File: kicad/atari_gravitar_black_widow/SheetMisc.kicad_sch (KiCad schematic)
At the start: 24 parts, among them J17 cat_box_con, J19 J19, J20 J20

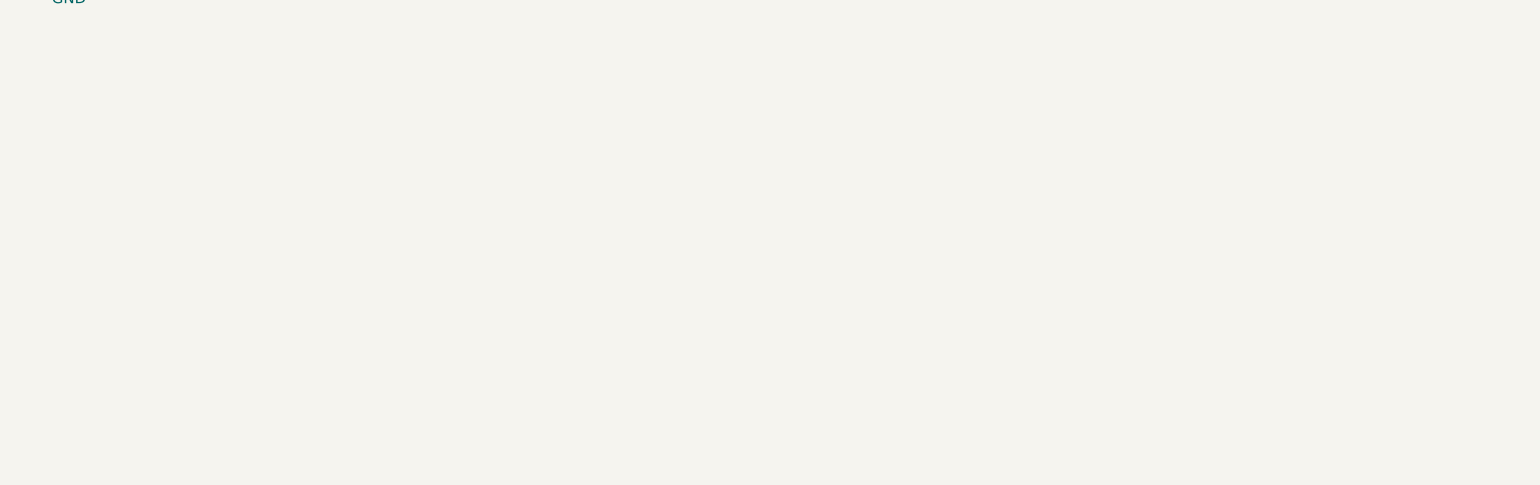
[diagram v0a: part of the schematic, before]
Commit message: NOT LOADED PARTS ADDED
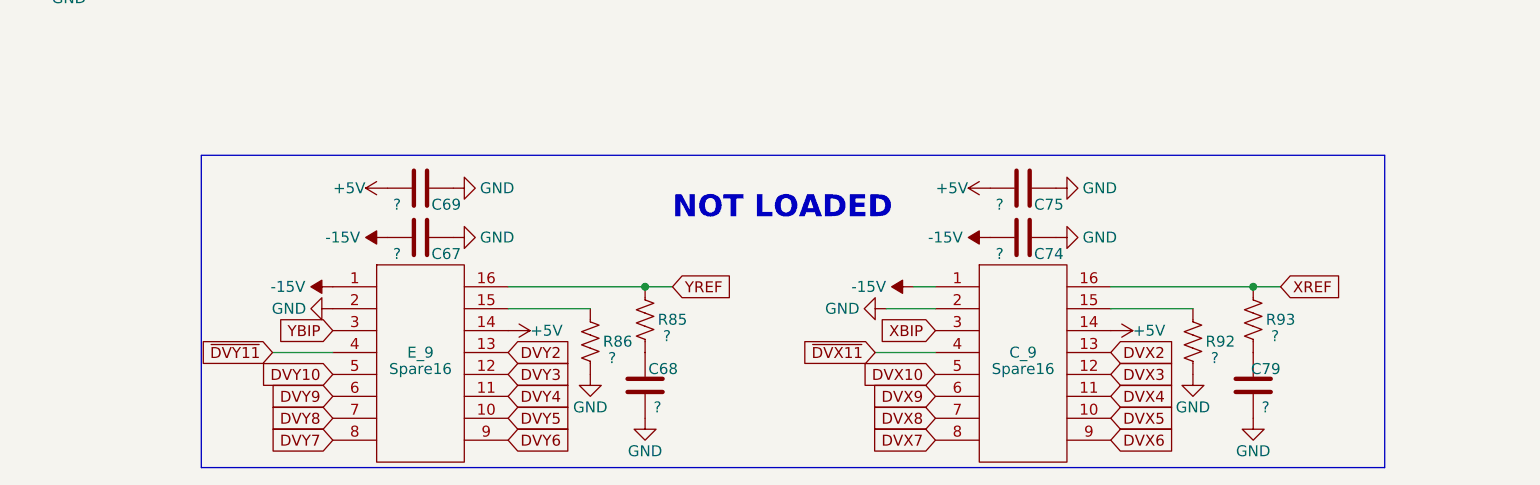
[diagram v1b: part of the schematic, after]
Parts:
- added C67, C69, C74, C75: ?, Star_Wars_Vector_PCB:GenericComp, symbol Device:C
- added C68, C79: ?, Star_Wars_Vector_PCB:CapBrown, symbol Device:C
- added C_9, E_9: Spare16, Star_Wars_Vector_PCB:DIP16, symbol quantum_arcade_pcb:Spare16
- added R85, R86, R92, R93: ?, Star_Wars_Vector_PCB:GenericComp, symbol Device:R_US
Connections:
- net +5V: now also C69.2, C75.2, C_9.14, E_9.14
- net GND: now also C67.1, C68.1, C69.1, C74.1, C75.1, C79.1, C_9.2, E_9.2, R86.1, R92.1
- new net: E_9.15, R86.2
- new net: C68.2, R85.1
- new net: C_9.15, R92.2
- new net: C79.2, R93.1
- new net -15V: C67.2, C74.2, C_9.1, E_9.1
- new net DVX10: C_9.5
- new net DVX2: C_9.13
- new net DVX3: C_9.12
- new net DVX4: C_9.11
- new net DVX5: C_9.10
- new net DVX6: C_9.9
- new net DVX7: C_9.8
- new net DVX8: C_9.7
- new net DVX9: C_9.6
- new net DVY10: E_9.5
- new net DVY2: E_9.13
- new net DVY3: E_9.12
- new net DVY4: E_9.11
- new net DVY5: E_9.10
- new net DVY6: E_9.9
- new net DVY7: E_9.8
- new net DVY8: E_9.7
- new net DVY9: E_9.6
- new net XBIP: C_9.3
- new net XREF: C_9.16, R93.2
- new net YBIP: E_9.3
- new net YREF: E_9.16, R85.2
- new net ~{DVX11}: C_9.4
- new net ~{DVY11}: E_9.4
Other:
- note added: "NOT LOADED"

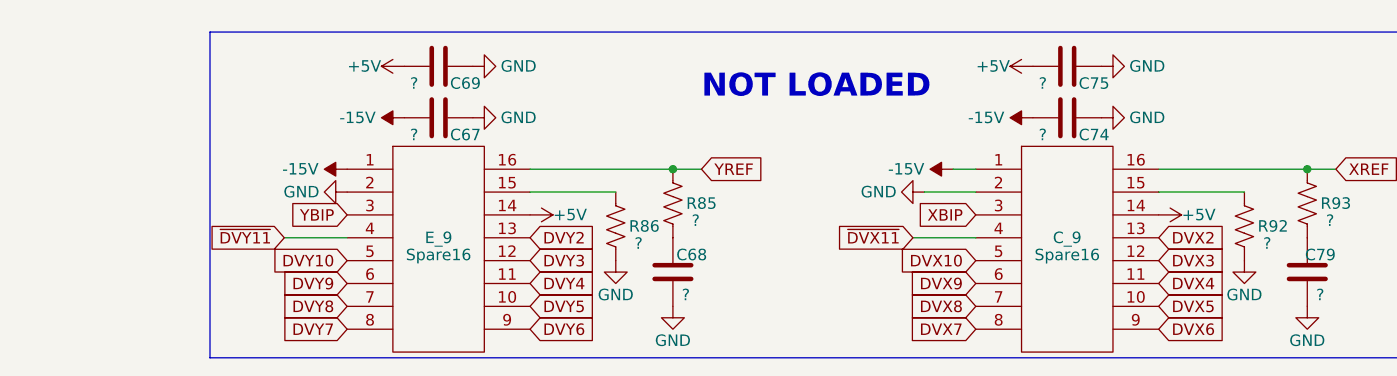
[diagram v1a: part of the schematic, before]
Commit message: unused parts places and traced
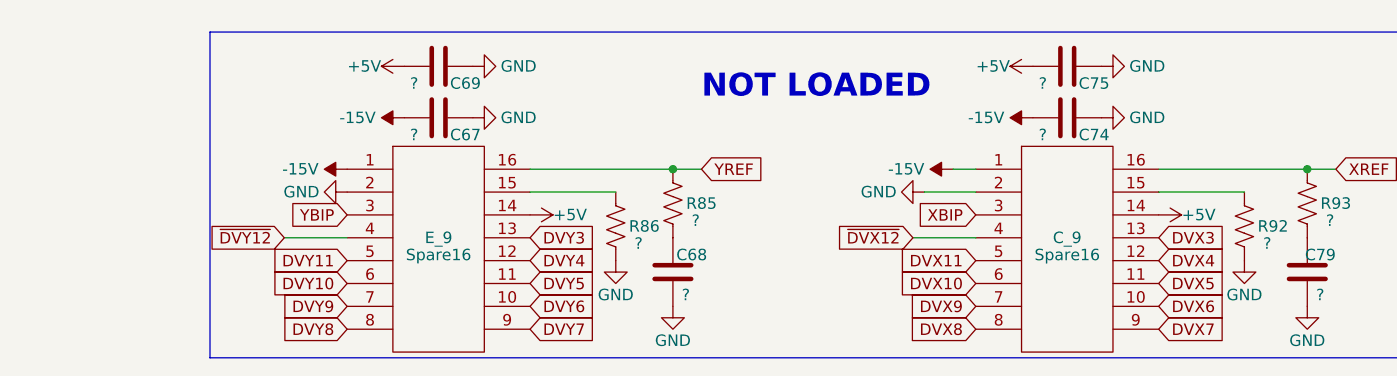
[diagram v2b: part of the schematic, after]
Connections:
- net DVX2 is gone; now on net DVX3: C_9.13
- net DVY2 is gone; now on net DVY3: E_9.13
- net DVX10: now also C_9.6; no longer C_9.5
- net DVX3: no longer C_9.12
- net DVX4: now also C_9.12; no longer C_9.11
- net DVX5: now also C_9.11; no longer C_9.10
- net DVX6: now also C_9.10; no longer C_9.9
- net DVX7: now also C_9.9; no longer C_9.8
- net DVX8: now also C_9.8; no longer C_9.7
- net DVX9: now also C_9.7; no longer C_9.6
- net DVY10: now also E_9.6; no longer E_9.5
- net DVY3: no longer E_9.12
- net DVY4: now also E_9.12; no longer E_9.11
- net DVY5: now also E_9.11; no longer E_9.10
- net DVY6: now also E_9.10; no longer E_9.9
- net DVY7: now also E_9.9; no longer E_9.8
- net DVY8: now also E_9.8; no longer E_9.7
- net DVY9: now also E_9.7; no longer E_9.6
- net ~{DVX11} renamed ~{DVX12}
- net ~{DVY11} renamed ~{DVY12}
- new net DVX11: C_9.5
- new net DVY11: E_9.5

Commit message: Fixed cat box connector
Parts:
- J17: footprint Asteroids:J21 -> Gravitar:catBox
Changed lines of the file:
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@@
     (property "Reference" "J17" (id 0) (at 137.16 24.765 0))
     (property "Value" "cat_box_con" (id 1) (at 122.555 24.765 0))
-    (property "Footprint" "Asteroids:J21" (id 2) (at 132.08 10.16 0)
+    (property "Footprint" "Gravitar:catBox" (id 2) (at 132.08 10.16 0)
       (effects (font (size 1.27 1.27)) hide)
     )
